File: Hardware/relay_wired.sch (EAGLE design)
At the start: 9 parts, among them K1 JJM1-12V

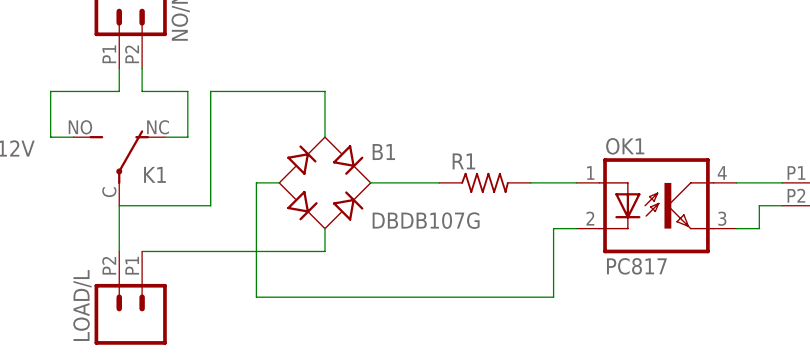
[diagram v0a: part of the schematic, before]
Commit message: Layout of board 33 x 33
Layout 33 x 33 board
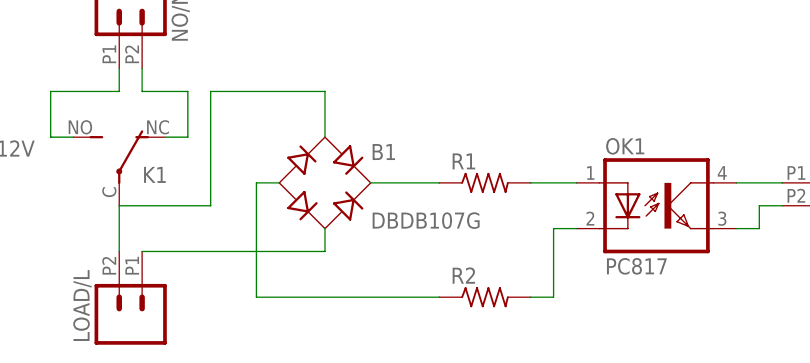
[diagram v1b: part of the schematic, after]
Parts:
- added R2: (no value), resistor:R-US_0207/10
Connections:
- new net N$10: OK1.C, R2.2
- net N$8: now also R2.1; no longer OK1.C
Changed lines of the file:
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@@
 <?xml version="1.0" encoding="utf-8"?>
 <!DOCTYPE eagle SYSTEM "eagle.dtd">
-<eagle version="7.3.0">
+<eagle version="7.7.0">
 <drawing>
 <settings>
@@
 <part name="OK1" library="optocoupler" deviceset="PC817" device=""/>
 <part name="S/GND" library="SparkFun-Connectors" deviceset="M02" device="2.54MM_SCREWTERM"/>
+<part name="R2" library="resistor" deviceset="R-US_" device="0207/10"/>
 </parts>
 <sheets>
@@
 <instance part="OK1" gate="A" x="137.16" y="71.12"/>
 <instance part="S/GND" gate="G$1" x="157.48" y="73.66" rot="R180"/>
+<instance part="R2" gate="G$1" x="116.84" y="60.96"/>
 </instances>
 <busses>
@@
 <wire x1="93.98" y1="73.66" x2="91.44" y2="73.66" width="0.1524" layer="91"/>
 <wire x1="91.44" y1="73.66" x2="91.44" y2="60.96" width="0.1524" layer="91"/>
-<wire x1="91.44" y1="60.96" x2="124.46" y2="60.96" width="0.1524" layer="91"/>
-<pinref part="OK1" gate="A" pin="C"/>
-<wire x1="127" y1="68.58" x2="124.46" y2="68.58" width="0.1524" layer="91"/>
-<wire x1="124.46" y1="68.58" x2="124.46" y2="60.96" width="0.1524" layer="91"/>
+<pinref part="R2" gate="G$1" pin="1"/>
+<wire x1="91.44" y1="60.96" x2="111.76" y2="60.96" width="0.1524" layer="91"/>
 </segment>
 </net>
@@
 </segment>
 </net>
+<net name="N$10" class="0">
+<segment>
+<pinref part="OK1" gate="A" pin="C"/>
+<wire x1="127" y1="68.58" x2="124.46" y2="68.58" width="0.1524" layer="91"/>
+<wire x1="124.46" y1="68.58" x2="124.46" y2="60.96" width="0.1524" layer="91"/>
+<pinref part="R2" gate="G$1" pin="2"/>
+<wire x1="121.92" y1="60.96" x2="124.46" y2="60.96" width="0.1524" layer="91"/>
+</segment>
+</net>

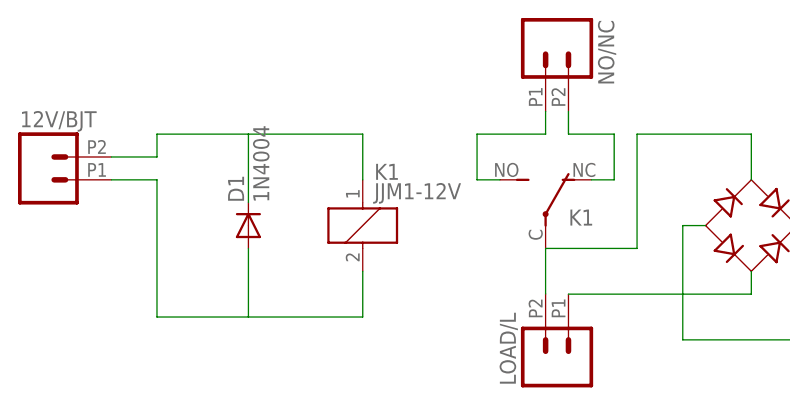
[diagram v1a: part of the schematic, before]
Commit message: Change layout to 25x40mm
- Change the layout to 25x40 mm since the max board size in the free eagle version is 160mm2 (100x80)
- Added text on pcb board layout and fixed trace width
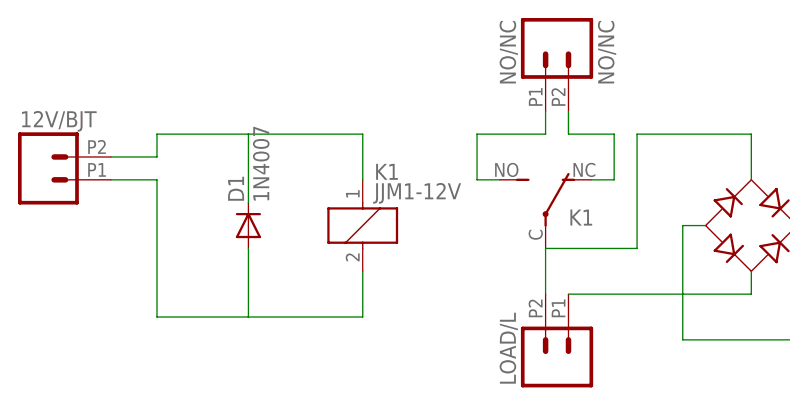
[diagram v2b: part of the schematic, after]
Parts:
- D1: value 1N4004 -> 1N4007
- NO/NC: value (none) -> NO/NC
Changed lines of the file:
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@@
 <parts>
 <part name="K1" library="relay" deviceset="JJM1-12V" device=""/>
-<part name="D1" library="adafruit" deviceset="1N4004" device=""/>
-<part name="NO/NC" library="SparkFun-Connectors" deviceset="M02" device="2.54MM_SCREWTERM"/>
+<part name="D1" library="adafruit" deviceset="1N4004" device="" value="1N4007"/>
+<part name="NO/NC" library="SparkFun-Connectors" deviceset="M02" device="2.54MM_SCREWTERM" value="NO/NC"/>
 <part name="12V/BJT" library="SparkFun-Connectors" deviceset="M02" device="2.54MM_SCREWTERM"/>
 <part name="LOAD/L" library="SparkFun-Connectors" deviceset="M02" device="2.54MM_SCREWTERM"/>

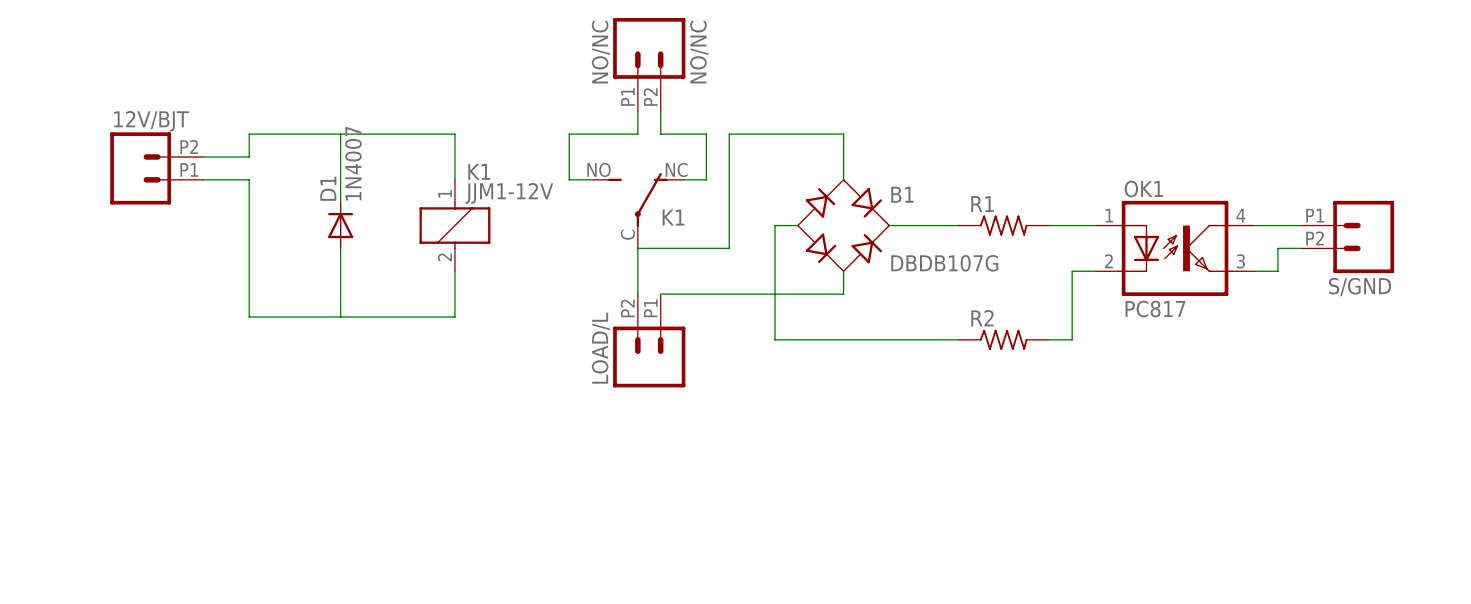
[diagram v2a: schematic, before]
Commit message: Branch for new design using SFH620A
Due to design layout size limitation - after fixing parts size - it was not possible to fit in the 25x40 layout a pc817 and a DB107 for detecting zero crossing. Thus this branch is to replace both with the SFH620A IC instead.

- Changed the terminal block size from 2.54 mm to 5 mm pith instead since this was available in the market.
- Changed the relay to SONGLE SRD-05VDC-SL-C design. Library is added also
- Changed resistors value to 0207/12 to fit 22k / 1W resistor value.
- Changed pic817 and DB107 with SFH620A
- reroute pcb layout again.

Todo: 
- Creepage 
- Double layer for high voltage side.
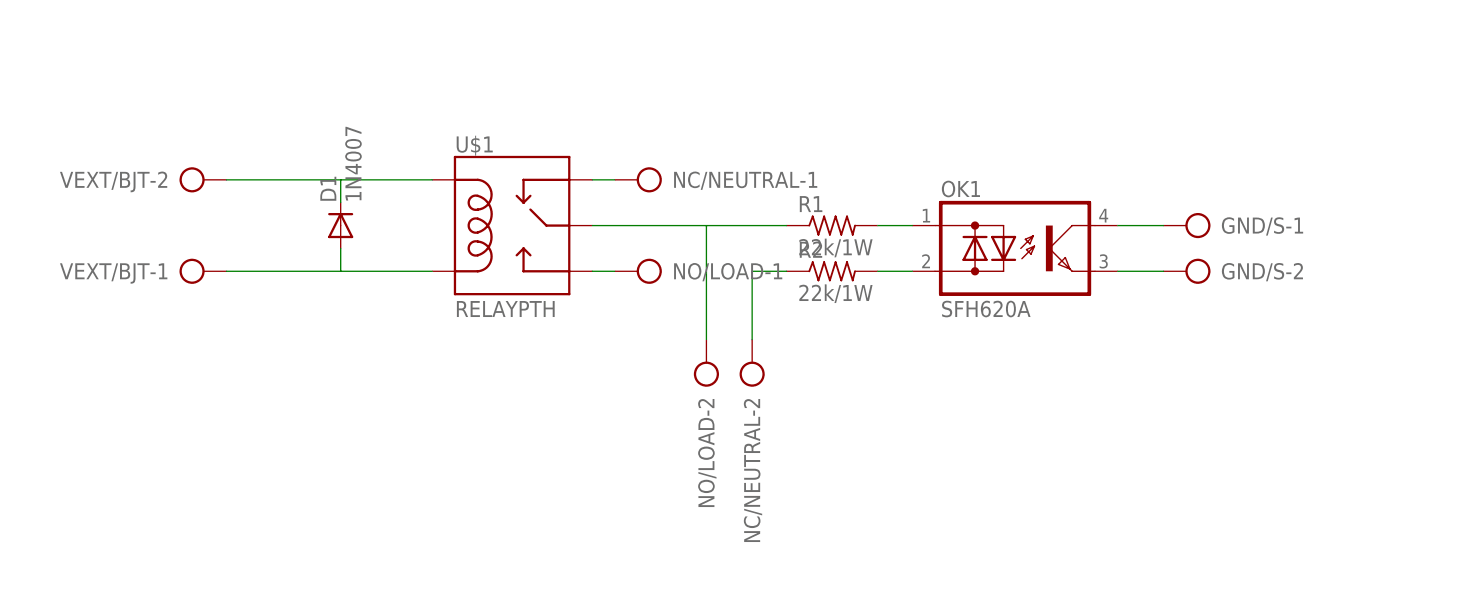
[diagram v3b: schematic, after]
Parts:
- removed 12V/BJT, LOAD/L, S/GND: (no value), SparkFun-Connectors:M022.54MM_SCREWTERM
- removed B1: DBDB107G, rectifier:DBDB107G
- removed K1: JJM1-12V, relay:JJM1-12V
- removed NO/NC: NO/NC, SparkFun-Connectors:M022.54MM_SCREWTERM
- added GND/S, NC/NEUTRAL, NO/LOAD, VEXT/BJT: (no value), con-ptr500:AK500/2
- added U$1: RELAYPTH, SRD-05VDC-SL-C:RELAYPTH
- OK1: value PC817 -> SFH620A; device optocoupler:PC817 -> optocoupler:SFH620A
- R1, R2: value (none) -> 22k/1W; device resistor:R-US_0207/10 -> rcl:R-US_0207/12
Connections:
- removed net N$10: OK1.C, R2.2
- removed net N$7: B1.AC2, LOAD/L.1
- removed net N$8: B1.-, R2.1
- new net N$13: D1.A, U$1.COIL0, VEXT/BJT-1.KL
- net N$1: now also U$1.COIL1, VEXT/BJT-2.KL; no longer 12V/BJT.2, K11.1
- net N$11: now also GND/S-1.KL, OK1.C; no longer OK1.COL, S/GND.1
- net N$12: now also GND/S-2.KL, OK1.E; no longer OK1.EMIT, S/GND.2
- net N$2: now also NC/NEUTRAL-1.KL, U$1.SWCLOSE; no longer 12V/BJT.1, D1.A, K11.2
- net N$3: now also NO/LOAD-1.KL, U$1.SWOPEN; no longer B1.AC1, K12.P, LOAD/L.2
- net N$4: now also NC/NEUTRAL-2.KL, R2.1; no longer K12.O, NO/NC.2
- net N$5: now also OK1.AC2, R2.2; no longer K12.S, NO/NC.1
- net N$6: now also OK1.AC1; no longer OK1.A
- net N$9: now also NO/LOAD-2.KL, U$1.SWCOMMON; no longer B1.+
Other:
- moved on the sheet: R1, R2

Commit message: Invert NC and NO name tags
Changes in schematic.
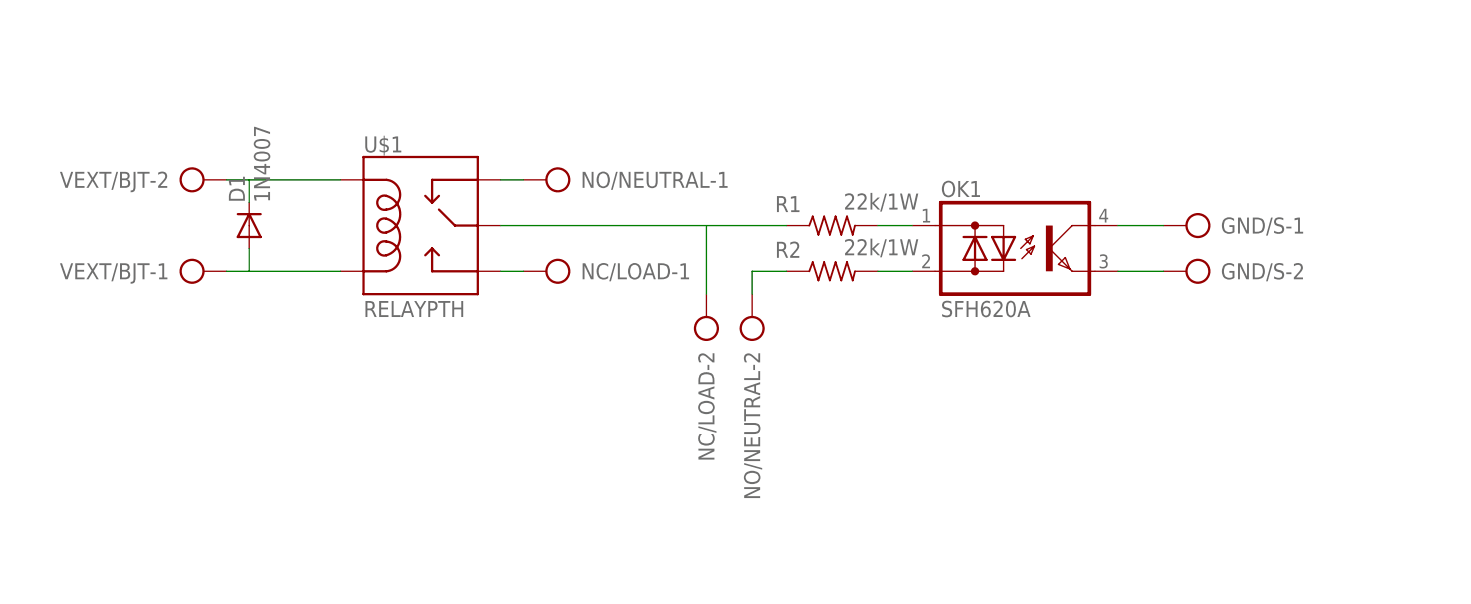
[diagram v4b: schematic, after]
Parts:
- removed NC/NEUTRAL, NO/LOAD: (no value), con-ptr500:AK500/2
- added NC/LOAD, NO/NEUTRAL: (no value), con-ptr500:AK500/2
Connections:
- net N$2: now also NO/NEUTRAL-1.KL; no longer NC/NEUTRAL-1.KL
- net N$3: now also NC/LOAD-1.KL; no longer NO/LOAD-1.KL
- net N$4: now also NO/NEUTRAL-2.KL; no longer NC/NEUTRAL-2.KL
- net N$9: now also NC/LOAD-2.KL; no longer NO/LOAD-2.KL
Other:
- moved on the sheet: D1, U$1
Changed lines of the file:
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@@
 <part name="R1" library="rcl" deviceset="R-US_" device="0207/12" value="22k/1W"/>
 <part name="R2" library="rcl" deviceset="R-US_" device="0207/12" value="22k/1W"/>
-<part name="NO/LOAD" library="con-ptr500" deviceset="AK500/2" device=""/>
+<part name="NC/LOAD" library="con-ptr500" deviceset="AK500/2" device=""/>
 <part name="VEXT/BJT" library="con-ptr500" deviceset="AK500/2" device=""/>
-<part name="NC/NEUTRAL" library="con-ptr500" deviceset="AK500/2" device=""/>
+<part name="NO/NEUTRAL" library="con-ptr500" deviceset="AK500/2" device=""/>
 <part name="GND/S" library="con-ptr500" deviceset="AK500/2" device=""/>
 <part name="U$1" library="SRD-05VDC-SL-C" deviceset="RELAY" device="PTH"/>
@@
 </plain>
 <instances>
-<instance part="D1" gate="1" x="43.18" y="73.66" rot="R90"/>
-<instance part="R1" gate="G$1" x="97.79" y="73.66"/>
-<instance part="R2" gate="G$1" x="97.79" y="68.58"/>
-<instance part="NO/LOAD" gate="-1" x="78.74" y="68.58" rot="R180"/>
-<instance part="NO/LOAD" gate="-2" x="83.82" y="55.88" rot="R90"/>
+<instance part="D1" gate="1" x="33.02" y="73.66" rot="R90"/>
+<instance part="R1" gate="G$1" x="97.79" y="73.66" smashed="yes">
+<attribute name="NAME" x="91.44" y="75.1586" size="1.778" layer="95"/>
+<attribute name="VALUE" x="99.06" y="75.438" size="1.778" layer="96"/>
+</instance>
+<instance part="R2" gate="G$1" x="97.79" y="68.58" smashed="yes">
+<attribute name="NAME" x="91.44" y="70.0786" size="1.778" layer="95"/>
+<attribute name="VALUE" x="99.06" y="70.358" size="1.778" layer="96"/>
+</instance>
+<instance part="NC/LOAD" gate="-1" x="68.58" y="68.58" rot="R180"/>
+<instance part="NC/LOAD" gate="-2" x="83.82" y="60.96" rot="R90"/>
 <instance part="VEXT/BJT" gate="-1" x="25.4" y="68.58"/>
 <instance part="VEXT/BJT" gate="-2" x="25.4" y="78.74"/>
-<instance part="NC/NEUTRAL" gate="-1" x="78.74" y="78.74" rot="R180"/>
-<instance part="NC/NEUTRAL" gate="-2" x="88.9" y="55.88" rot="R90"/>
+<instance part="NO/NEUTRAL" gate="-1" x="68.58" y="78.74" rot="R180"/>
+<instance part="NO/NEUTRAL" gate="-2" x="88.9" y="60.96" rot="R90"/>
 <instance part="GND/S" gate="-1" x="139.7" y="73.66" rot="R180"/>
 <instance part="GND/S" gate="-2" x="139.7" y="68.58" rot="R180"/>
-<instance part="U$1" gate="G$1" x="63.5" y="73.66"/>
+<instance part="U$1" gate="G$1" x="53.34" y="73.66"/>
 <instance part="OK1" gate="G$1" x="116.84" y="71.12"/>
 </instances>
@@
 <segment>
 <pinref part="D1" gate="1" pin="C"/>
-<wire x1="43.18" y1="76.2" x2="43.18" y2="78.74" width="0.1524" layer="91"/>
+<wire x1="33.02" y1="76.2" x2="33.02" y2="78.74" width="0.1524" layer="91"/>
 <pinref part="U$1" gate="G$1" pin="COIL1"/>
-<wire x1="43.18" y1="78.74" x2="53.34" y2="78.74" width="0.1524" layer="91"/>
+<wire x1="33.02" y1="78.74" x2="43.18" y2="78.74" width="0.1524" layer="91"/>
 <pinref part="VEXT/BJT" gate="-2" pin="KL"/>
-<wire x1="30.48" y1="78.74" x2="43.18" y2="78.74" width="0.1524" layer="91"/>
+<wire x1="30.48" y1="78.74" x2="33.02" y2="78.74" width="0.1524" layer="91"/>
 </segment>
 </net>
@@
 <pinref part="R1" gate="G$1" pin="1"/>
 <pinref part="U$1" gate="G$1" pin="SWCOMMON"/>
-<wire x1="71.12" y1="73.66" x2="83.82" y2="73.66" width="0.1524" layer="91"/>
-<pinref part="NO/LOAD" gate="-2" pin="KL"/>
+<wire x1="60.96" y1="73.66" x2="83.82" y2="73.66" width="0.1524" layer="91"/>
+<pinref part="NC/LOAD" gate="-2" pin="KL"/>
 <wire x1="83.82" y1="73.66" x2="92.71" y2="73.66" width="0.1524" layer="91"/>
-<wire x1="83.82" y1="60.96" x2="83.82" y2="73.66" width="0.1524" layer="91"/>
+<wire x1="83.82" y1="66.04" x2="83.82" y2="73.66" width="0.1524" layer="91"/>
 </segment>
 </net>
@@
 <segment>
 <pinref part="D1" gate="1" pin="A"/>
-<wire x1="43.18" y1="71.12" x2="43.18" y2="68.58" width="0.1524" layer="91"/>
+<wire x1="33.02" y1="71.12" x2="33.02" y2="68.58" width="0.1524" layer="91"/>
 <pinref part="U$1" gate="G$1" pin="COIL0"/>
-<wire x1="53.34" y1="68.58" x2="43.18" y2="68.58" width="0.1524" layer="91"/>
+<wire x1="43.18" y1="68.58" x2="33.02" y2="68.58" width="0.1524" layer="91"/>
 <pinref part="VEXT/BJT" gate="-1" pin="KL"/>
-<wire x1="43.18" y1="68.58" x2="30.48" y2="68.58" width="0.1524" layer="91"/>
+<wire x1="33.02" y1="68.58" x2="30.48" y2="68.58" width="0.1524" layer="91"/>
 </segment>
 </net>
@@
 <segment>
 <pinref part="U$1" gate="G$1" pin="SWOPEN"/>
-<pinref part="NO/LOAD" gate="-1" pin="KL"/>
-<wire x1="71.12" y1="68.58" x2="73.66" y2="68.58" width="0.1524" layer="91"/>
+<pinref part="NC/LOAD" gate="-1" pin="KL"/>
+<wire x1="60.96" y1="68.58" x2="63.5" y2="68.58" width="0.1524" layer="91"/>
 </segment>
 </net>
@@
 <segment>
 <pinref part="R2" gate="G$1" pin="1"/>
-<pinref part="NC/NEUTRAL" gate="-2" pin="KL"/>
+<pinref part="NO/NEUTRAL" gate="-2" pin="KL"/>
 <wire x1="92.71" y1="68.58" x2="88.9" y2="68.58" width="0.1524" layer="91"/>
-<wire x1="88.9" y1="68.58" x2="88.9" y2="60.96" width="0.1524" layer="91"/>
+<wire x1="88.9" y1="68.58" x2="88.9" y2="66.04" width="0.1524" layer="91"/>
 </segment>
 </net>
@@
 <segment>
 <pinref part="U$1" gate="G$1" pin="SWCLOSE"/>
-<pinref part="NC/NEUTRAL" gate="-1" pin="KL"/>
-<wire x1="71.12" y1="78.74" x2="73.66" y2="78.74" width="0.1524" layer="91"/>
+<pinref part="NO/NEUTRAL" gate="-1" pin="KL"/>
+<wire x1="60.96" y1="78.74" x2="63.5" y2="78.74" width="0.1524" layer="91"/>
 </segment>
 </net>

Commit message: Branching for Omron G5Q-1-EU DC12 relay
- Replaced relay to Omron G5Q-1-EU DC12
- Board size reduced from 40x25 to 32x25
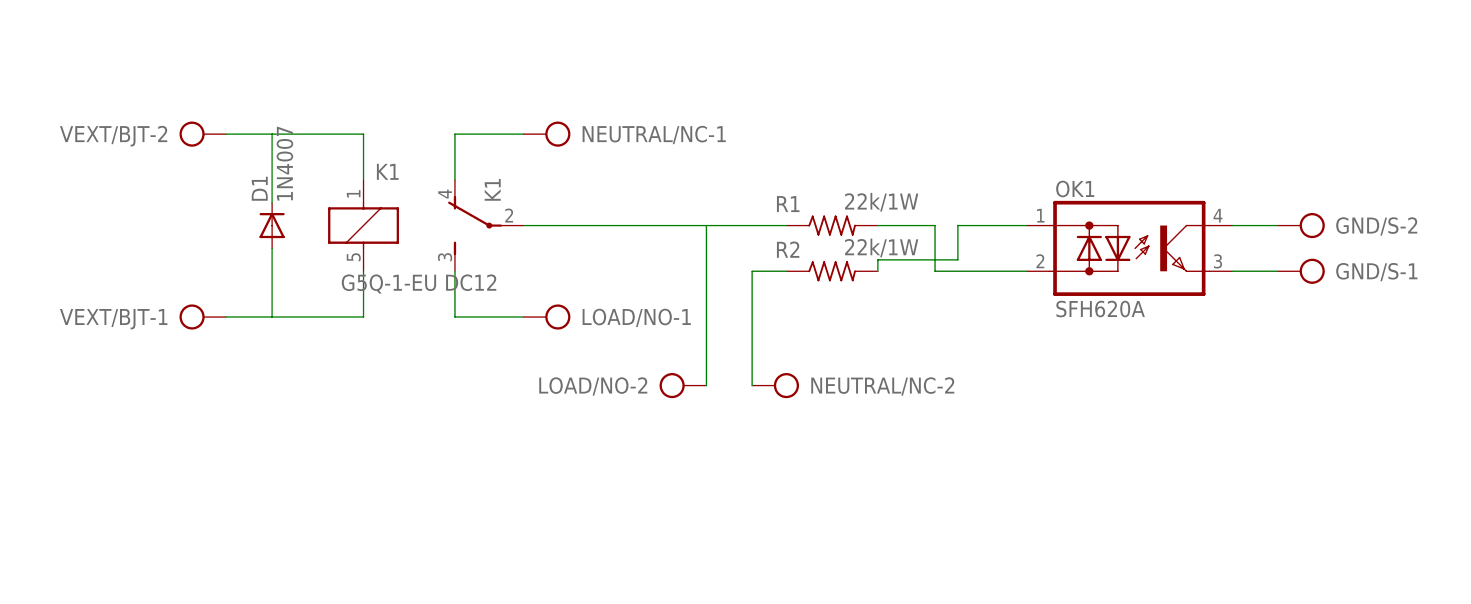
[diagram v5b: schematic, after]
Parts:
- removed NC/LOAD, NO/NEUTRAL: (no value), con-ptr500:AK500/2
- removed U$1: RELAYPTH, SRD-05VDC-SL-C:RELAYPTH
- added K1: G5Q-1-EU DC12, relay:G5SB
- added LOAD/NO, NEUTRAL/NC: (no value), con-ptr500-modified:AK500/2
- D1: device adafruit:1N4004 -> diode:DIODE-D-7.5
- GND/S, VEXT/BJT: device con-ptr500:AK500/2 -> con-ptr500-modified:AK500/2
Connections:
- removed net N$13: D1.A, U$1.COIL0, VEXT/BJT-1.KL
- removed net N$3: NC/LOAD-1.KL, U$1.SWOPEN
- removed net N$5: OK1.AC2, R2.2
- removed net N$6: OK1.AC1, R1.2
- new net N$10: GND/S-1.KL, OK1.E
- new net N$14: K1U.S, LOAD/NO-1.KL
- new net N$15: K1U.O, NEUTRAL/NC-1.KL
- new net N$8: GND/S-2.KL, OK1.C
- net N$1: now also OK1.AC1, R2.2; no longer D1.C, U$1.COIL1, VEXT/BJT-2.KL
- net N$11: now also D1.C, K11.1, VEXT/BJT-2.KL; no longer GND/S-1.KL, OK1.C
- net N$12: now also D1.A, K11.2, VEXT/BJT-1.KL; no longer GND/S-2.KL, OK1.E
- net N$2: now also OK1.AC2, R1.2; no longer NO/NEUTRAL-1.KL, U$1.SWCLOSE
- net N$4: now also NEUTRAL/NC-2.KL; no longer NO/NEUTRAL-2.KL
- net N$9: now also K1U.P, LOAD/NO-2.KL; no longer NC/LOAD-2.KL, U$1.SWCOMMON
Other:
- moved on the sheet: GND/S-1, GND/S-2, OK1, VEXT/BJT-1, VEXT/BJT-2

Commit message: [BUG] Relay was set to mirror by mistake
- A major bug while reviewing where the relay was set to mirror. 
- Updated gerb274x.cam to generate silk screen for bottom also
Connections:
- removed net N$11: D1.C, K11.1, VEXT/BJT-2.KL
- removed net N$12: D1.A, K11.2, VEXT/BJT-1.KL
- removed net N$14: K1U.S, LOAD/NO-1.KL
- new net N$6: K1U.S, LOAD/NO-2.KL
- new net N$7: D1.C, K11.1, VEXT/BJT-1.KL
- new net N$8: D1.A, K11.2, VEXT/BJT-2.KL
- net N$1: now also OK1.AC2; no longer OK1.AC1
- net N$2: now also OK1.AC1; no longer OK1.AC2
- net N$9: now also LOAD/NO-1.KL; no longer LOAD/NO-2.KL
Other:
- moved on the sheet: D1, GND/S-1, GND/S-2, LOAD/NO-1, LOAD/NO-2, VEXT/BJT-1, VEXT/BJT-2
